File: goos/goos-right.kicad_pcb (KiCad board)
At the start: 2 copper layers, 140.2 x 108.1 mm, 22 parts

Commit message: feat: right side routed
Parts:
- U1: moved to B.Cu
- moved JP1 3.51 mm to (235.0, 39.5)
- turned J1 to 180 degrees
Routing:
- net D0: track 0.00 -> 177.3 mm
- net D4: track 0.00 -> 163.0 mm
- net D2: track 0.00 -> 152.7 mm
- net D15: track 0.00 -> 145.9 mm
- net D5: track 0.00 -> 145.9 mm
- net D6: track 0.00 -> 139.2 mm
- net D1: track 0.00 -> 137.8 mm
- net D3: track 0.00 -> 135.1 mm
- net D18: track 0.00 -> 132.3 mm
- net D10: track 0.00 -> 111.3 mm
- net D16: track 0.00 -> 97.4 mm
- net D14: track 0.00 -> 83.4 mm
- net D7: track 0.00 -> 61.5 mm
- net Net-(J1-B+): track 0.00 -> 60.5 mm, vias 0 -> 1
- net Net-(U1-B+): track 0.00 -> 60.3 mm, vias 0 -> 1
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- added copper zone on B.Cu, net GND
- added copper zone on F.Cu, net GND

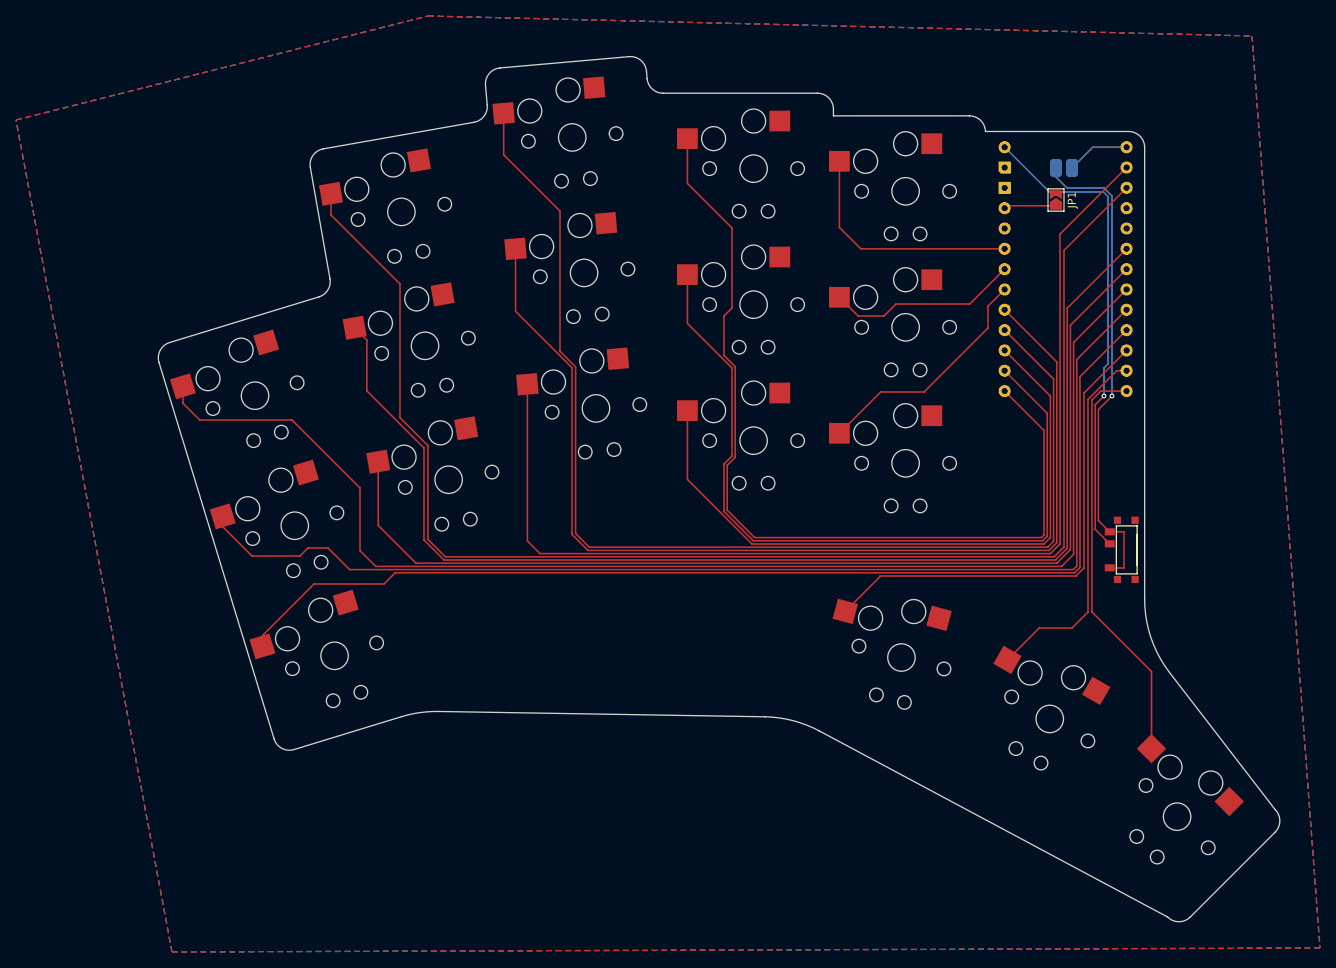
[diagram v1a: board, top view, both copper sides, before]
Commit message: feat: right side rounded and filled
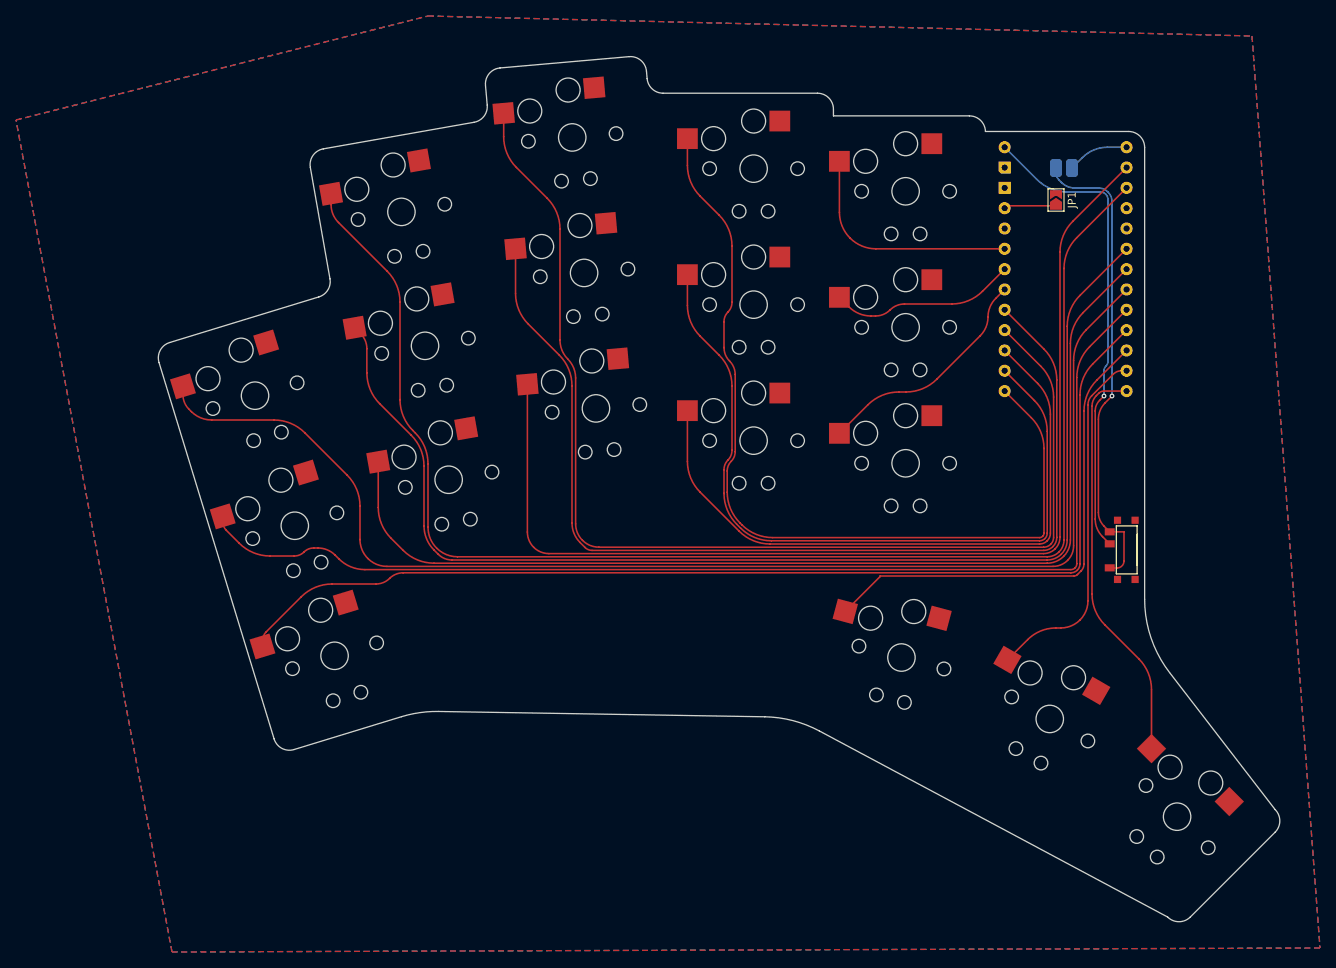
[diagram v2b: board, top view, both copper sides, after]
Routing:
- net D10: track 111.3 -> 109.4 mm
- net D0: track 177.3 -> 175.5 mm
- net D4: track 163.0 -> 161.3 mm
- net D16: track 97.4 -> 95.8 mm
- net D15: track 145.9 -> 144.4 mm
- net D2: track 152.7 -> 151.2 mm
- net D5: track 145.9 -> 144.7 mm
- net D18: track 132.3 -> 131.1 mm
- net D3: track 135.1 -> 134.0 mm
- net Net-(J1-B+): track 60.5 -> 59.4 mm
- net D6: track 139.2 -> 138.2 mm
- net D14: track 83.4 -> 82.5 mm
- net D19: track 29.7 -> 28.9 mm
- net D1: track 137.8 -> 137.1 mm
- net D8: track 45.4 -> 44.7 mm
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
